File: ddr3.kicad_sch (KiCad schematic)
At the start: 61 parts, among them U7 AS4C256M16D3, U8 TPS51200DRC

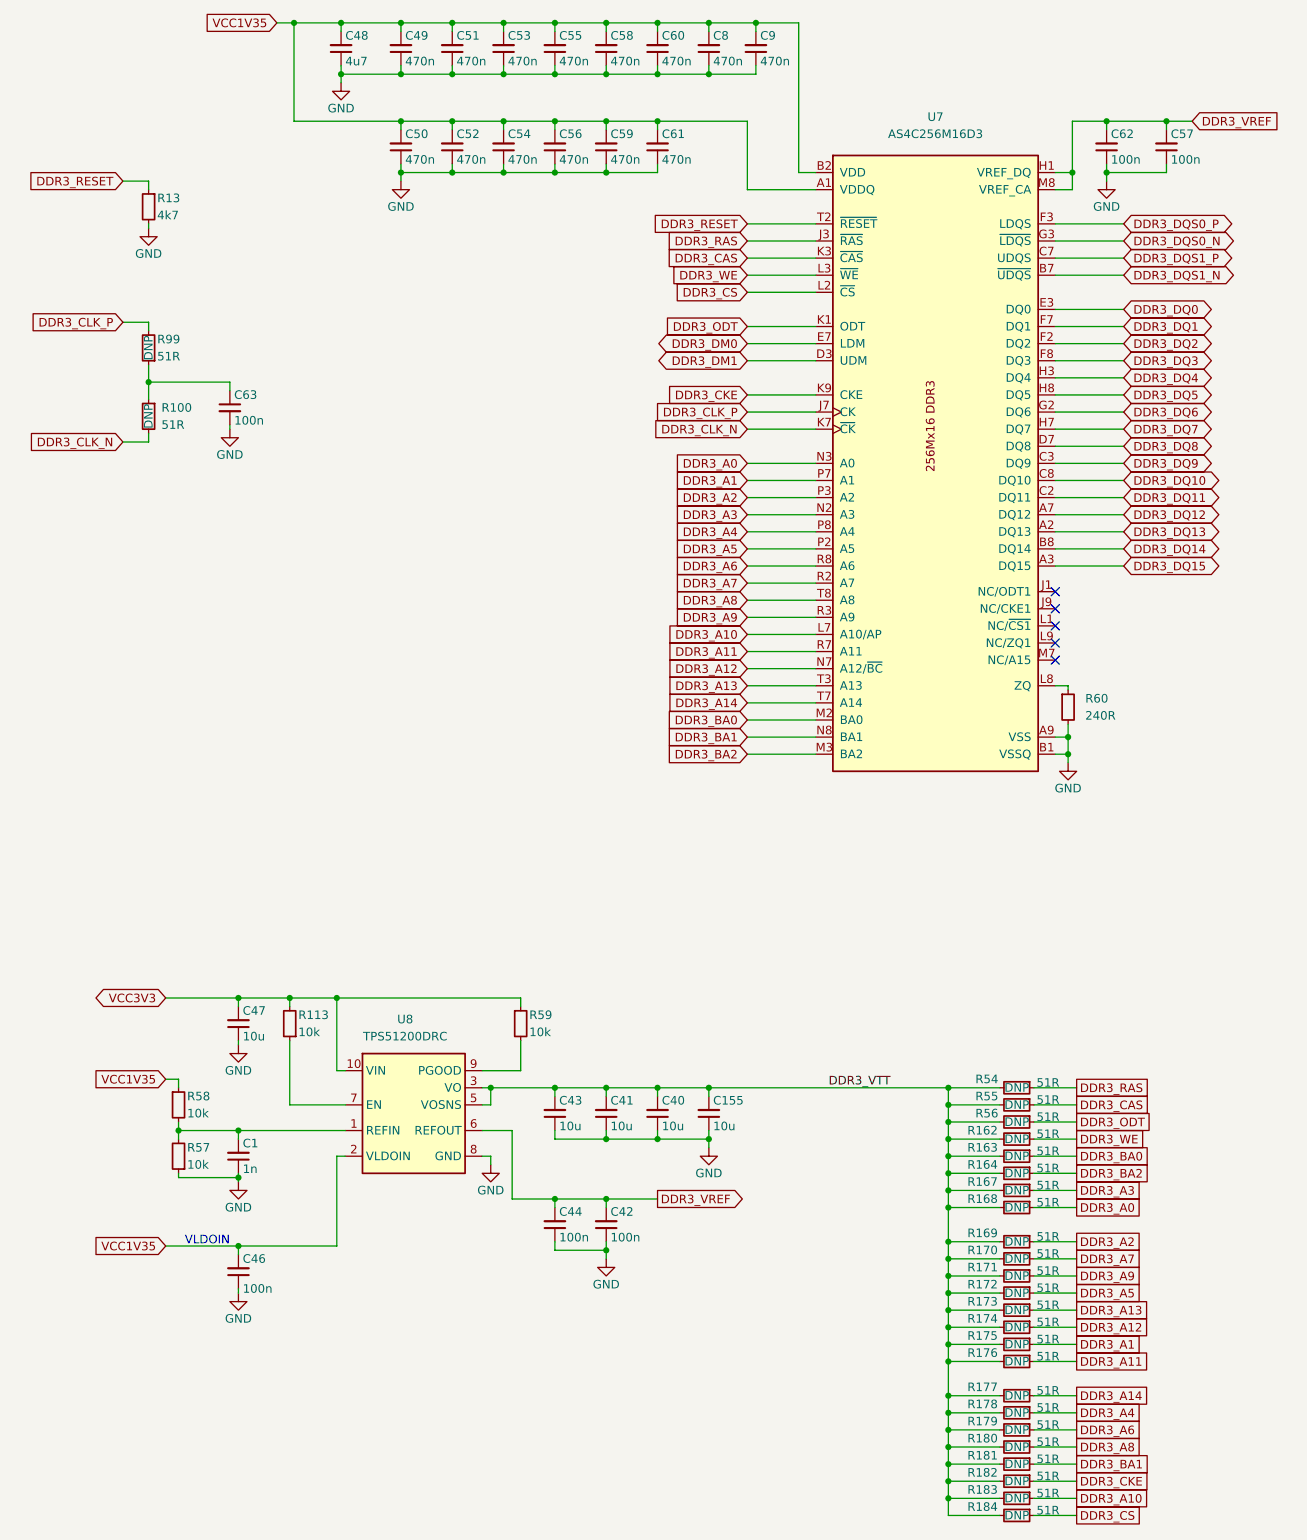
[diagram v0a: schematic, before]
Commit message: [#55652] Fix hotareas
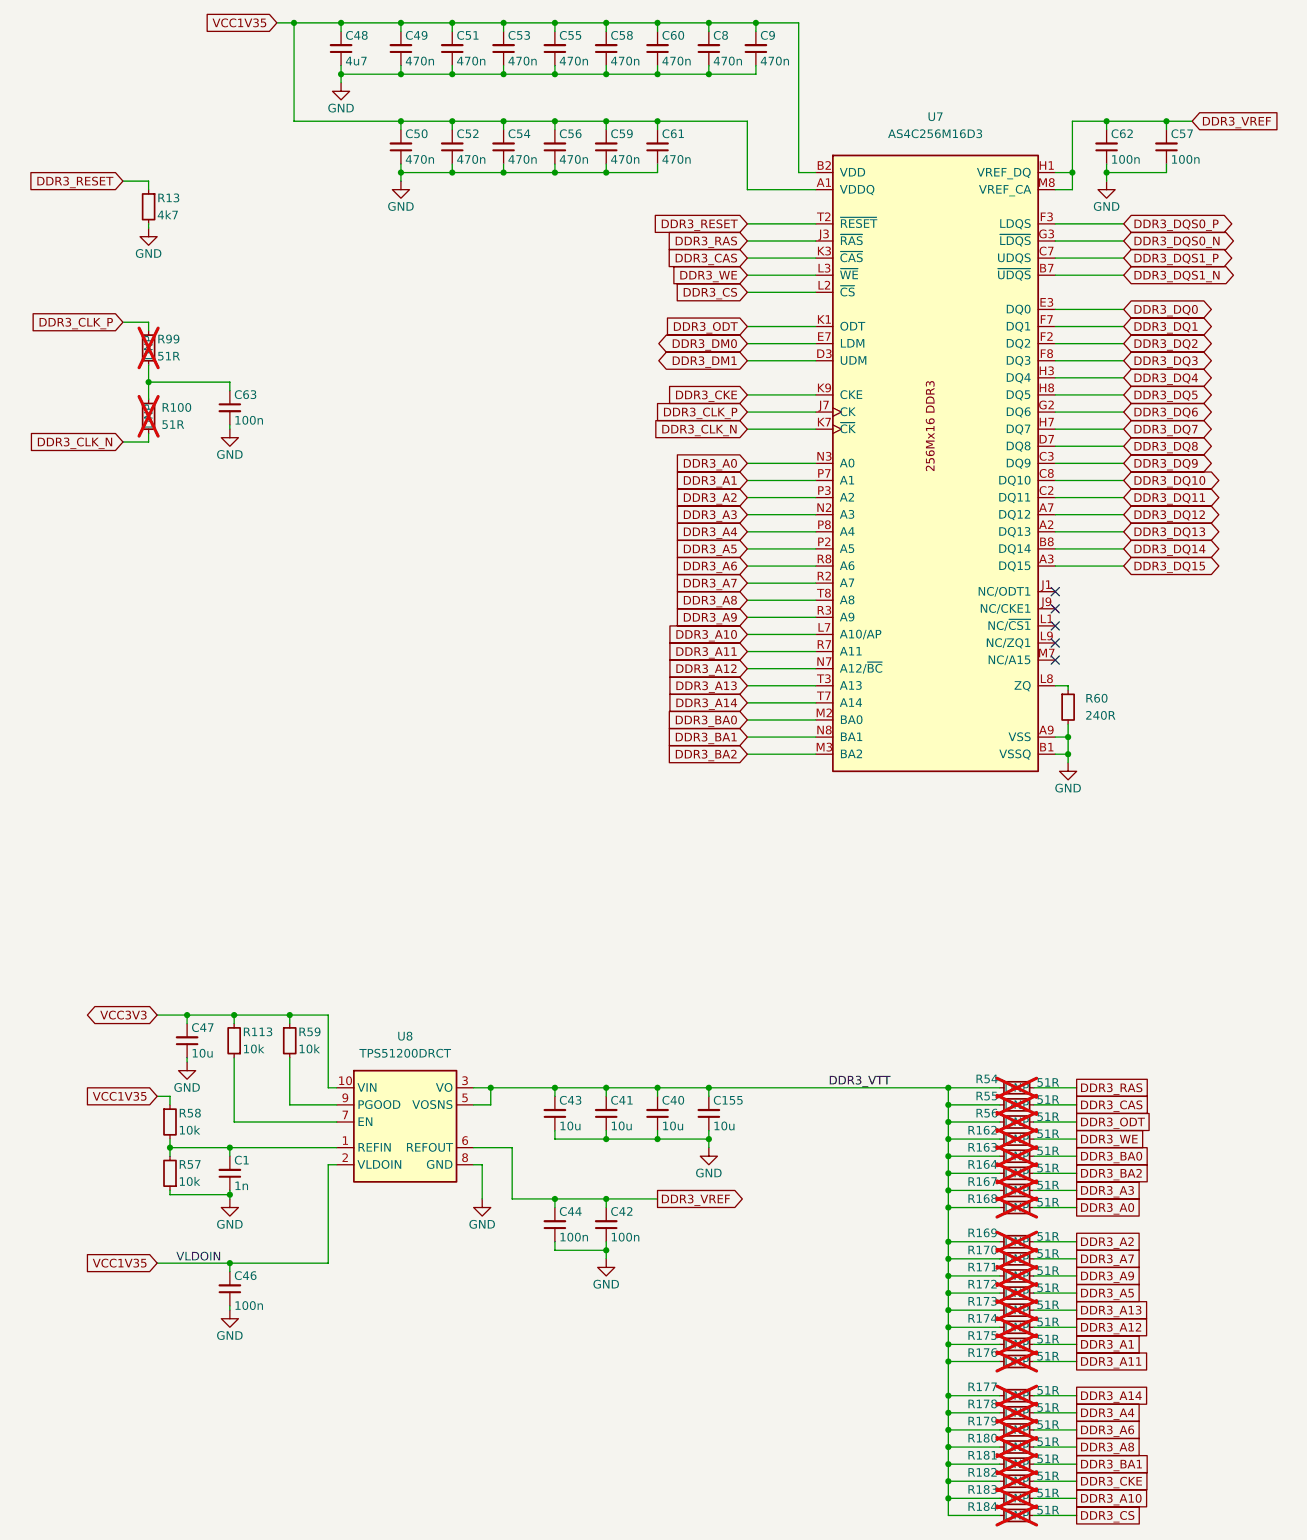
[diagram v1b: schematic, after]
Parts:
- C155, C40, C41, C43, C47: Manufacturer Yaego -> YAGEO
- R100, R162, R163, R164, R167, R168, R169, R170, R171, R172, R173, R174, R175, R176, R177, R178, R179, R180, R181, R182, R183, R184, R54, R55, R56, R99: now not fitted; now left out of the parts list
- U8: value TPS51200DRC -> TPS51200DRCT; symbol antmicroPMICVoltageRegulatorsDCDCSwitchingControllers:TPS51200DRC -> antmicroPMICVoltageRegulatorsDCDCSwitchingControllers:TPS51200DRCT; MPN TPS51200DRC -> TPS51200DRCT; VSD_class (none) -> TPS51200
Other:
- moved on the sheet: C1, C46, C47, R113, R57, R58, R59, U8

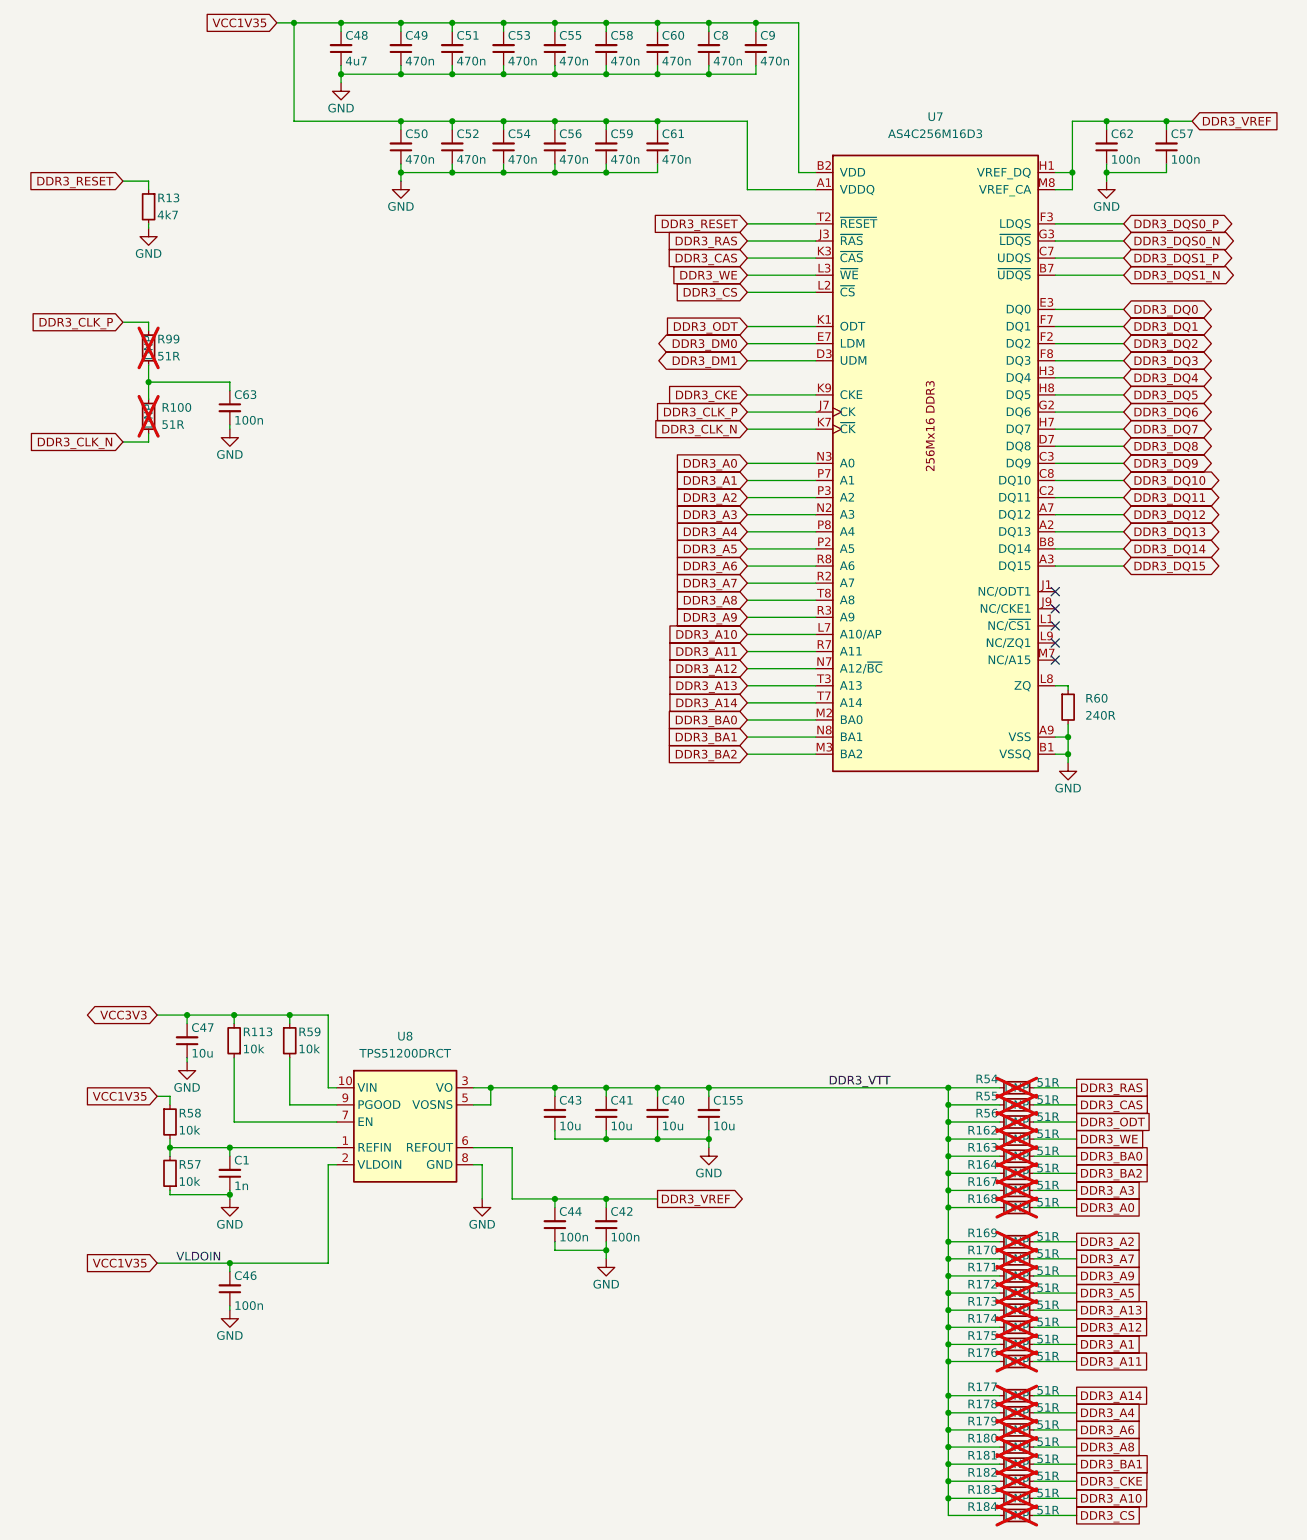
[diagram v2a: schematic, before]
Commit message: [#68236] Allign sch to grid
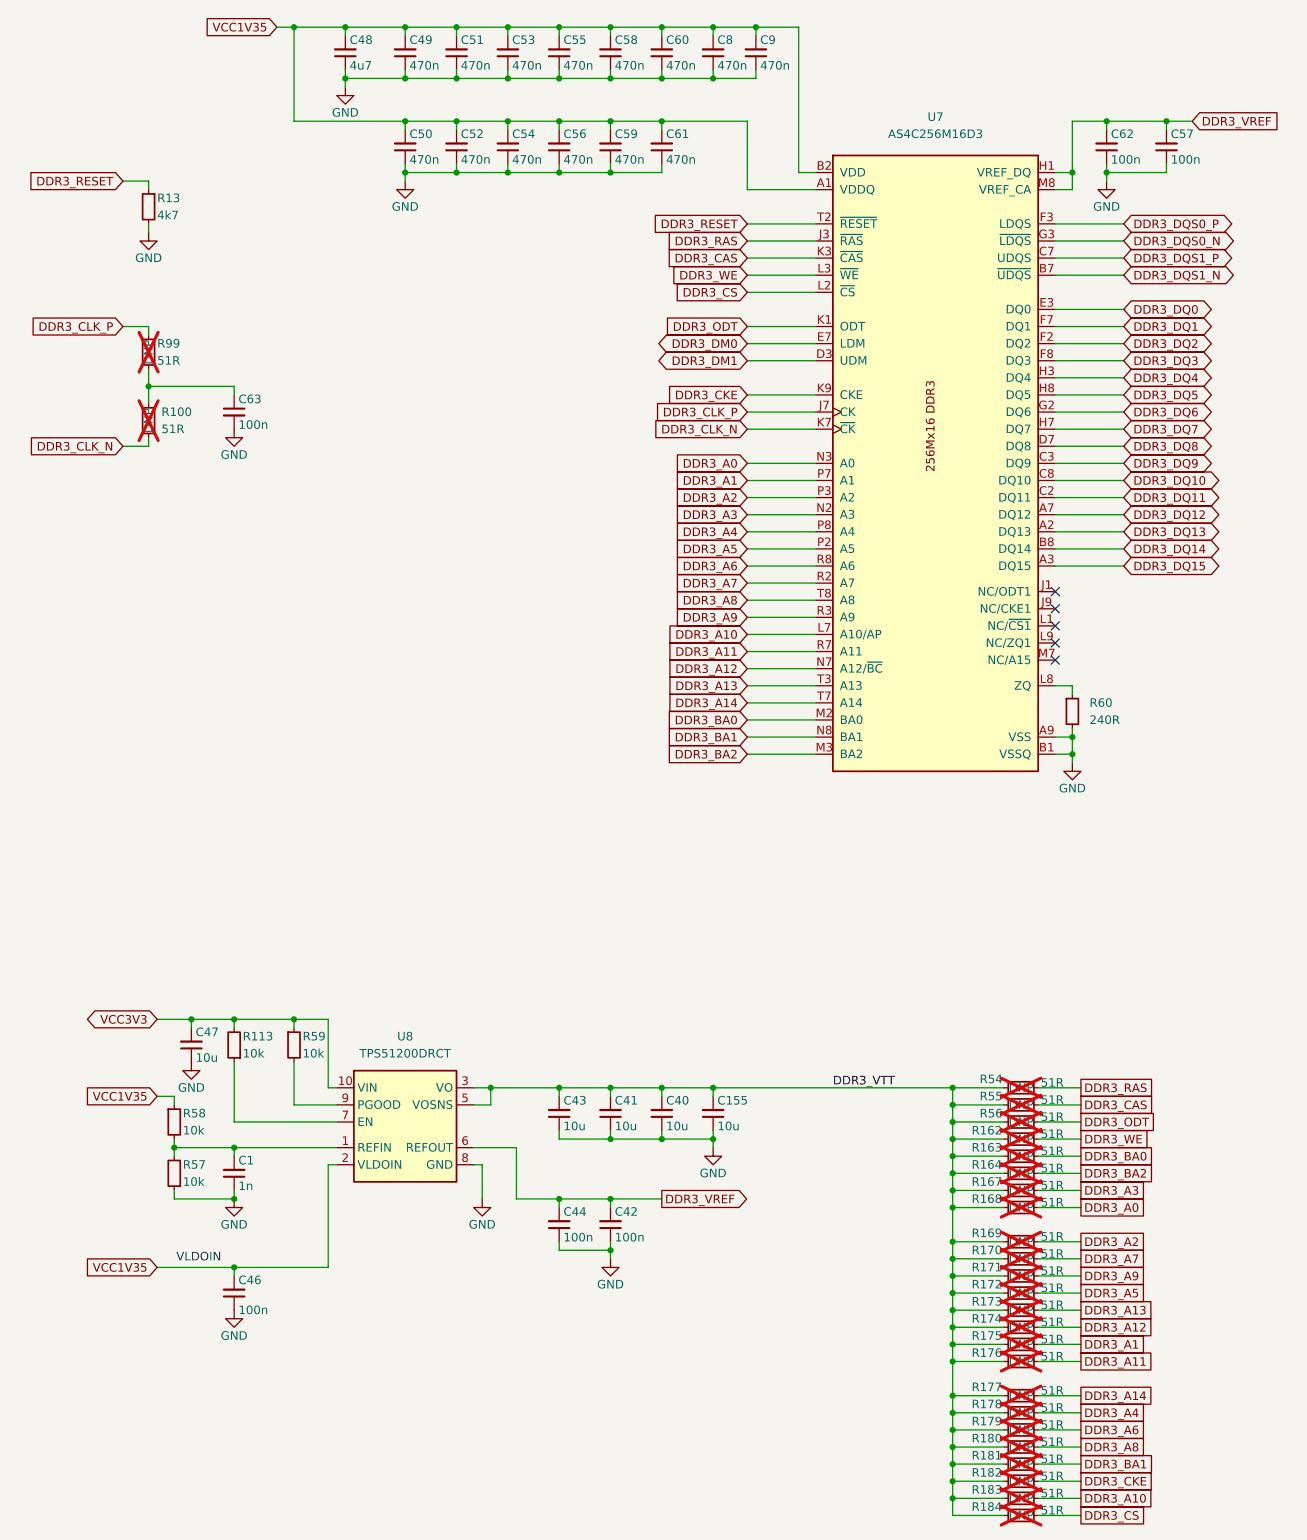
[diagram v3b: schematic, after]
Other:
- moved on the sheet: C1, C155, C40, C41, C42, C43, C44, C46, C47, C48, C49, C50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
